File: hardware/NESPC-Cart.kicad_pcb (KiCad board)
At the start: 4 copper layers, 165.7 x 100 mm, 33 parts, among them J0 NESCART, J1 HOST, J2 FLOPPY, J3 EXPANSION, J4 FLOPPY, J5 HOST, J6 JTAG, U1 FDC37C78, U2 CLONE CIC, U3 ATF1508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

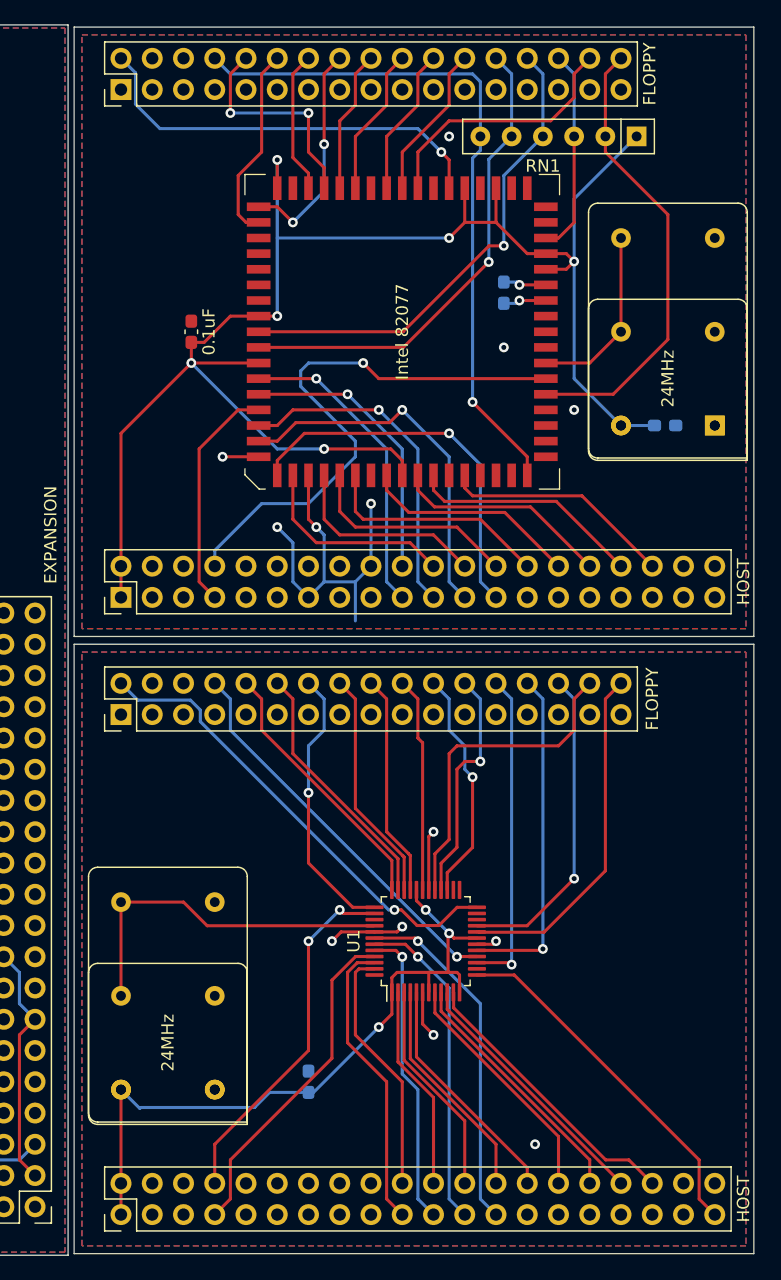
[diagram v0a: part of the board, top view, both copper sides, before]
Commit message: Intel 82077 FDC and more rework
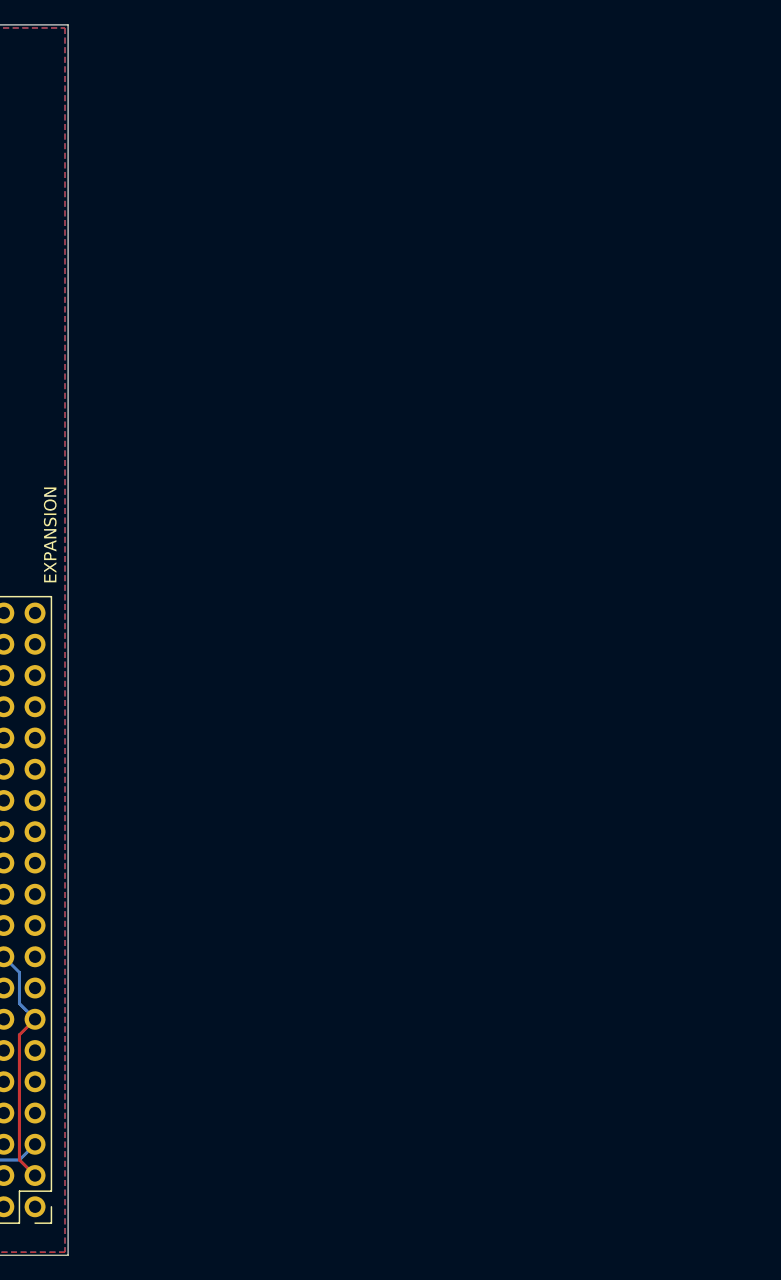
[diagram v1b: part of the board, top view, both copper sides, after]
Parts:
- removed C1, C11, C13: 0.1uF, Capacitor_SMD:C_0603_1608Metric_Pad1.08x0.95mm_HandSolder
- removed C12: 4.7pF, Capacitor_SMD:C_0603_1608Metric_Pad1.08x0.95mm_HandSolder
- removed J1, J5: HOST, Connector_PinHeader_2.54mm:PinHeader_2x20_P2.54mm_Vertical
- removed J2, J4: FLOPPY, Connector_PinHeader_2.54mm:PinHeader_2x17_P2.54mm_Vertical
- removed RN1: 1Kx5, Resistor_THT:R_Array_SIP6
- removed U1: FDC37C78, Package_QFP:LQFP-48_7x7mm_P0.5mm
- removed U4: Intel 82077, Package_LCC:PLCC-68
- removed X1, X4: 24MHz, Oscillator:Oscillator_DIP-8
- removed X2, X3: CXO_DIP14, Oscillator:Oscillator_DIP-14
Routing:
- net /Floppy Disk Controller 82077/+5V: track 137.1 -> 0.00 mm, vias 6 -> 0
- net /Floppy Disk Controller 37C78/+5V: track 58.4 -> 0.00 mm, vias 3 -> 0
- net /Floppy Disk Controller 82077/FLP_~INDEX: track 56.5 -> 0.00 mm, vias 1 -> 0
- net /Floppy Disk Controller 82077/FDC_RST: track 45.4 -> 0.00 mm, vias 1 -> 0
- net /Floppy Disk Controller 82077/FLP_~WRTPRT: track 39.9 -> 0.00 mm, vias 1 -> 0
- net /Floppy Disk Controller 82077/FLP_~TRK0: track 39.4 -> 0.00 mm, vias 1 -> 0
- net /Floppy Disk Controller 37C78/FLP_DENSEL: track 38.2 -> 0.00 mm, vias 1 -> 0
- net /Floppy Disk Controller 82077/FLP_~DSKCHG: track 37.2 -> 0.00 mm
- net /Floppy Disk Controller 82077/FLP_DENSEL: track 33.9 -> 0.00 mm, vias 1 -> 0
- net /Floppy Disk Controller 82077/GND: track 33.3 -> 0.00 mm, vias 7 -> 0
- net /Floppy Disk Controller 37C78/FLP_~INDEX: track 32.0 -> 0.00 mm, vias 1 -> 0
- net /Floppy Disk Controller 82077/CPU_A2: track 31.0 -> 0.00 mm, vias 1 -> 0
- net /Floppy Disk Controller 82077/CPU_A1: track 30.1 -> 0.00 mm, vias 1 -> 0
- net /Floppy Disk Controller 37C78/FDC_RST: track 29.4 -> 0.00 mm, vias 2 -> 0
- net /Floppy Disk Controller 37C78/~IRQ: track 29.3 -> 0.00 mm
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- removed copper zone on B.Cu, net /Floppy Disk Controller 37C78/GND
- removed copper zone on F.Cu, net /Floppy Disk Controller 37C78/GND
- removed copper zone on B.Cu, net /Floppy Disk Controller 82077/GND
- removed copper zone on F.Cu, net /Floppy Disk Controller 82077/GND
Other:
- board size 165.7 x 100 mm -> 110 x 100 mm

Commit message: Pin remapping final final final really this time
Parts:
- U2: value CLONE CIC -> CIC
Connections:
- J6 pad 2: /TMS -> /TDI
- J6 pad 3: /TCK -> /TMS
- J6 pad 5: /TDI -> /TCK
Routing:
- net /TDI: track 15.8 -> 8.17 mm
- net /TCK: track 47.0 -> 50.7 mm
- net /TDO: track 52.3 -> 50.3 mm
- net /TMS: track 17.4 -> 18.4 mm
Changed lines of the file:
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@@
     (thickness 1.6)
     (drawings 31)
-    (tracks 1164)
+    (tracks 1167)
     (zones 0)
     (modules 18)
@@
     (mod_text_size 1 1)
     (mod_text_width 0.15)
-    (pad_size 1.6 1.6)
-    (pad_drill 0.8)
+    (pad_size 1.7 1.7)
+    (pad_drill 1)
     (pad_to_mask_clearance 0)
     (aux_axis_origin 0 0)
@@
       (usegerberattributes true)
       (usegerberadvancedattributes true)
-      (creategerberjobfile true)
+      (creategerberjobfile false)
       (excludeedgelayer true)
       (linewidth 0.100000)
@@
       (drillshape 0)
       (scaleselection 1)
-      (outputdirectory "NC-Gerbers/"))
+      (outputdirectory "NC-Gerbers/CART"))
   )
   (net 0 "")
@@
       (effects (font (size 1 1) (thickness 0.15)))
     )
-    (fp_text value "CLONE CIC" (at 3.81 3.81 90) (layer F.SilkS)
+    (fp_text value CIC (at 3.81 3.81 90) (layer F.SilkS)
       (effects (font (size 1 1) (thickness 0.15)))
     )
@@
     (descr "32-lead though-hole mounted DIP package, row spacing 15.24 mm (600 mils)")
     (tags "THT DIP DIL PDIP 2.54mm 15.24mm 600mil")
-    (fp_text reference U8 (at 7.62 -2.33 90) (layer F.SilkS)
-      (effects (font (size 1 1) (thickness 0.15)))
-    )
-    (fp_text value "512Kx8 FLASH CHR" (at 7.62 40.43 90) (layer F.Fab)
+    (fp_text reference U8 (at 7.62 0.635 90) (layer F.Fab) hide
+      (effects (font (size 1 1) (thickness 0.15)))
+    )
+    (fp_text value "512Kx8 FLASH CHR" (at 7.62 19.05 180) (layer F.SilkS)
       (effects (font (size 1 1) (thickness 0.15)))
     )
@@
     (fp_line (start 14.985 -1.27) (end 14.985 39.37) (layer F.Fab) (width 0.1))
     (fp_line (start 1.255 -1.27) (end 14.985 -1.27) (layer F.Fab) (width 0.1))
-    (fp_text user %R (at 7.62 19.05 90) (layer F.Fab)
+    (fp_text user %R (at 7.62 0.635 90) (layer F.Fab) hide
       (effects (font (size 1 1) (thickness 0.15)))
     )
@@
     )
   )
-  (module Connector_PinHeader_2.54mm:PinHeader_1x06_P2.54mm_Vertical locked (layer F.Cu)
+  (module Connector_PinHeader_2.54mm:PinHeader_1x06_P2.54mm_Vertical (layer F.Cu)
     (at 135.255 125.73 90)
     (descr "Through hole straight pin header, 1x06, 2.54mm pitch, single row")
@@
       (net 1 /GND))
     (pad 5 thru_hole oval (at 0 10.16 90) (size 1.7 1.7) (drill 1) (layers *.Cu *.Mask)
-      (net 85 /TDI))
+      (net 83 /TCK))
     (pad 4 thru_hole oval (at 0 7.62 90) (size 1.7 1.7) (drill 1) (layers *.Cu *.Mask)
       (net 82 /TDO))
     (pad 3 thru_hole oval (at 0 5.08 90) (size 1.7 1.7) (drill 1) (layers *.Cu *.Mask)
-      (net 83 /TCK))
+      (net 84 /TMS))
     (pad 2 thru_hole oval (at 0 2.54 90) (size 1.7 1.7) (drill 1) (layers *.Cu *.Mask)
-      (net 84 /TMS))
+      (net 85 /TDI))
     (pad 1 thru_hole circle (at 0 0 90) (size 1.7 1.7) (drill 1) (layers *.Cu *.Mask)
       (net 37 /+5V))
@@
     (effects (font (size 1 1) (thickness 0.2)))
   )
-  (gr_text TDI (at 145.415 130.175) (layer F.SilkS)
+  (gr_text TDI (at 137.795 128.27) (layer F.SilkS)
     (effects (font (size 1 1) (thickness 0.2)))
   )
@@
     (effects (font (size 1 1) (thickness 0.2)))
   )
-  (gr_text TCK (at 140.335 130.175) (layer F.SilkS)
+  (gr_text TCK (at 145.415 130.175) (layer F.SilkS)
     (effects (font (size 1 1) (thickness 0.2)))
   )
-  (gr_text TMS (at 137.795 128.905) (layer F.SilkS)
+  (gr_text TMS (at 140.335 130.175) (layer F.SilkS)
     (effects (font (size 1 1) (thickness 0.2)))
   )
@@
   (segment (start 126.365 107.315) (end 125.104978 108.575022) (width 0.25) (layer F.Cu) (net 81) (status 40000))
   (segment (start 130.4175 107.315) (end 126.365 107.315) (width 0.25) (layer F.Cu) (net 81) (status 40010))
-  (segment (start 142.875 121.92) (end 142.875 125.73) (width 0.25) (layer In2.Cu) (net 82) (status 40020))
-  (segment (start 113.120024 113.03) (end 133.985 113.03) (width 0.25) (layer In2.Cu) (net 82) (status 40000))
-  (segment (start 104.185012 121.965012) (end 113.120024 113.03) (width 0.25) (layer In2.Cu) (net 82) (status 40000))
-  (segment (start 133.985 113.03) (end 142.875 121.92) (width 0.25) (layer In2.Cu) (net 82) (status 40000))
   (segment (start 103.595024 122.555) (end 101.9925 122.555) (width 0.25) (layer F.Cu) (net 82) (status 40020))
   (segment (start 104.185012 121.965012) (end 103.595024 122.555) (width 0.25) (layer F.Cu) (net 82) (status 40000))
   (via (at 104.185012 121.965012) (size 0.8) (drill 0.4) (layers F.Cu B.Cu) (net 82) (status 40000))
-  (via (at 114.3 113.75501) (size 0.8) (drill 0.4) (layers F.Cu B.Cu) (net 83) (status 40000))
-  (segment (start 101.9925 111.125) (end 112.395 111.125) (width 0.25) (layer F.Cu) (net 83) (status 40010))
-  (segment (start 114.3 113.03) (end 114.3 113.75501) (width 0.25) (layer F.Cu) (net 83) (status 40000))
-  (segment (start 112.395 111.125) (end 114.3 113.03) (width 0.25) (layer F.Cu) (net 83) (status 40000))
-  (segment (start 140.335 125.73) (end 140.335 121.92) (width 0.25) (layer In2.Cu) (net 83) (status 40010))
-  (segment (start 140.335 121.92) (end 132.17001 113.75501) (width 0.25) (layer In2.Cu) (net 83) (status 40000))
-  (segment (start 132.17001 113.75501) (end 114.3 113.75501) (width 0.25) (layer In2.Cu) (net 83) (status 40000))
+  (segment (start 142.875 124.46) (end 142.875 125.73) (width 0.25) (layer In2.Cu) (net 82))
+  (segment (start 132.08 113.665) (end 142.875 124.46) (width 0.25) (layer In2.Cu) (net 82))
+  (segment (start 124.46 113.665) (end 132.08 113.665) (width 0.25) (layer In2.Cu) (net 82))
+  (segment (start 123.19 114.935) (end 124.46 113.665) (width 0.25) (layer In2.Cu) (net 82))
+  (segment (start 111.215024 114.935) (end 123.19 114.935) (width 0.25) (layer In2.Cu) (net 82))
+  (segment (start 104.185012 121.965012) (end 111.215024 114.935) (width 0.25) (layer In2.Cu) (net 82))
+  (segment (start 120.015 111.125) (end 122.555 113.665) (width 0.25) (layer F.Cu) (net 83))
+  (segment (start 101.9925 111.125) (end 120.015 111.125) (width 0.25) (layer F.Cu) (net 83))
+  (via (at 122.555 113.665) (size 0.8) (drill 0.4) (layers F.Cu B.Cu) (net 83))
+  (segment (start 123.19 113.03) (end 122.555 113.665) (width 0.25) (layer In2.Cu) (net 83))
+  (segment (start 133.985 113.03) (end 123.19 113.03) (width 0.25) (layer In2.Cu) (net 83))
+  (segment (start 145.415 124.46) (end 133.985 113.03) (width 0.25) (layer In2.Cu) (net 83))
+  (segment (start 145.415 125.73) (end 145.415 124.46) (width 0.25) (layer In2.Cu) (net 83))
   (segment (start 132.080006 112.395) (end 130.4175 112.395) (width 0.25) (layer F.Cu) (net 84) (status 40020))
   (segment (start 137.795 121.285) (end 137.795 118.109994) (width 0.25) (layer F.Cu) (net 84) (status 40000))
-  (segment (start 137.795 125.73) (end 137.795 121.285) (width 0.25) (layer In2.Cu) (net 84) (status 40010))
   (segment (start 137.795 118.109994) (end 132.080006 112.395) (width 0.25) (layer F.Cu) (net 84) (status 40000))
   (via (at 137.795 121.285) (size 0.8) (drill 0.4) (layers F.Cu B.Cu) (net 84) (status 40000))
-  (segment (start 143.51 123.825) (end 145.415 125.73) (width 0.25) (layer F.Cu) (net 85) (status 40020))
-  (segment (start 130.4175 123.825) (end 143.51 123.825) (width 0.25) (layer F.Cu) (net 85) (status 40010))
+  (segment (start 137.795 123.19) (end 140.335 125.73) (width 0.25) (layer In2.Cu) (net 84))
+  (segment (start 137.795 121.285) (end 137.795 123.19) (width 0.25) (layer In2.Cu) (net 84))
+  (segment (start 135.89 123.825) (end 137.795 125.73) (width 0.25) (layer F.Cu) (net 85))
+  (segment (start 130.4175 123.825) (end 135.89 123.825) (width 0.25) (layer F.Cu) (net 85))
   (via (at 135.255 102.87) (size 0.8) (drill 0.4) (layers F.Cu B.Cu) (net 88) (status 40000))
   (segment (start 136.525 104.14) (end 135.255 102.87) (width 0.25) (layer In1.Cu) (net 88) (status 40000))

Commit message: Finalized boards sent out for Rev.0
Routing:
- net /GND: track 73.8 -> 64.7 mm, vias 21 -> 32
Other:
- board text added: "JLCJLCJLCJLC"
